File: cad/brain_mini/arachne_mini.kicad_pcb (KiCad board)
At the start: 4 copper layers, 92 x 60 mm, 86 parts, among them J1 12V IN, J13 5V PI, J2 L1 servo, J3 L2 servo, J4 L3 servo, J5 L4 servo, J6 L5 servo, J7 L6 servo, J8 USB-C PI, Q1 AOD4185, SW1 RESET, SW2 BOOT, U1 TPS54560B, U10 USBLC6-2SC6, U2 AMS1117-3.3, U3 ESP32-S3-WROOM-1-N16R8, U4 74AHCT1G126, U5 74LVC1G34, U6 74AHCT1G126, U7 74LVC1G34, U8 MPU-6050

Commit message: Mini board: 2x13 GPIO header with all 19 free ESP32-S3 GPIOs + I2C + power, IMU moved
Co-Authored-By: Claude Opus 5.5 <noreply@anthropic.com>
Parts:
- added J14: GPIO, arachne:PinHeader_2x13_P2.54mm_Vertical, F.Cu at (151.2, 93.5)
- moved C24 17.6 mm to (147.0, 87.0)
- moved C25 17.6 mm to (154.0, 87.0)
- moved C26 17.6 mm to (154.0, 83.0)
- moved C27 17.6 mm to (147.0, 83.0)
- moved R24 17.6 mm to (156.0, 83.0)
- moved R25 17.6 mm to (157.6, 83.0)
- moved U8 17.6 mm to (150.5, 85.0)
- moved D6 2.50 mm to (160.0, 117.5)
- moved D7 2.50 mm to (160.0, 121.5)
- moved R27 1.30 mm to (164.8, 118.5)
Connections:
- U3 pad 12: unconnected-(U3-IO8-Pad12) -> IO8
- U3 pad 15: unconnected-(U3-IO3-Pad15) -> IO3
- U3 pad 16: unconnected-(U3-IO46-Pad16) -> IO46
- U3 pad 20: unconnected-(U3-IO12-Pad20) -> IO12
- U3 pad 21: unconnected-(U3-IO13-Pad21) -> IO13
- U3 pad 22: unconnected-(U3-IO14-Pad22) -> IO14
- U3 pad 23: unconnected-(U3-IO21-Pad23) -> IO21
- U3 pad 24: unconnected-(U3-IO47-Pad24) -> IO47
- U3 pad 25: unconnected-(U3-IO48-Pad25) -> IO48
- U3 pad 26: unconnected-(U3-IO45-Pad26) -> IO45
- U3 pad 31: unconnected-(U3-IO38-Pad31) -> IO38
- U3 pad 32: unconnected-(U3-IO39-Pad32) -> IO39
- U3 pad 33: unconnected-(U3-IO40-Pad33) -> IO40
- U3 pad 34: unconnected-(U3-IO41-Pad34) -> IO41
- U3 pad 35: unconnected-(U3-IO42-Pad35) -> IO42
- U3 pad 36: unconnected-(U3-RXD0-Pad36) -> IO44
- U3 pad 37: unconnected-(U3-TXD0-Pad37) -> IO43
- U3 pad 7: unconnected-(U3-IO7-Pad7) -> IO7
- U3 pad 8: unconnected-(U3-IO15-Pad8) -> IO15
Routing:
- net IO44: track 0.00 -> 70.6 mm, vias 0 -> 1
- net IO40: track 0.00 -> 69.2 mm, vias 0 -> 1
- net IO42: track 0.00 -> 69.2 mm, vias 0 -> 1
- net IO43: track 0.00 -> 66.5 mm, vias 0 -> 1
- net IO41: track 0.00 -> 61.7 mm, vias 0 -> 1
- net IO39: track 0.00 -> 59.8 mm, vias 0 -> 1
- net IO38: track 0.00 -> 56.3 mm, vias 0 -> 2
- net IO48: track 0.00 -> 53.8 mm, vias 0 -> 1
- net IO45: track 0.00 -> 42.6 mm, vias 0 -> 2
- net IO21: track 0.00 -> 34.7 mm, vias 0 -> 2
- net IO14: track 0.00 -> 34.1 mm, vias 0 -> 3
- net IO47: track 0.00 -> 33.6 mm, vias 0 -> 2
- net IO46: track 0.00 -> 32.4 mm, vias 0 -> 1
- net IO13: track 0.00 -> 31.1 mm, vias 0 -> 2
- net IO7: track 0.00 -> 26.4 mm, vias 0 -> 1
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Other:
- board text added: "3V3"
- board text added: "5V"
- board text added: "GND"
- board text added: "GPIO"
- board text added: "IO12"
- board text added: "IO13"
- board text added: "IO14"
- board text added: "IO15"
- board text added: "IO21"
- board text added: "IO3"
- board text added: "IO38"
- board text added: "IO39"
- board text added: "IO40"
- board text added: "IO41"
- board text added: "IO42"
- board text added: "IO45"
- board text added: "IO46"
- board text added: "IO47"
- board text added: "IO48"
- board text added: "IO7"
- board text added: "IO8"
- board text added: "RX44"
- board text added: "SCL5"
- board text added: "SDA4"
- board text added: "TX43"
- board text removed: "ESP32-S3 v1.0"
- board text removed: "MINI"

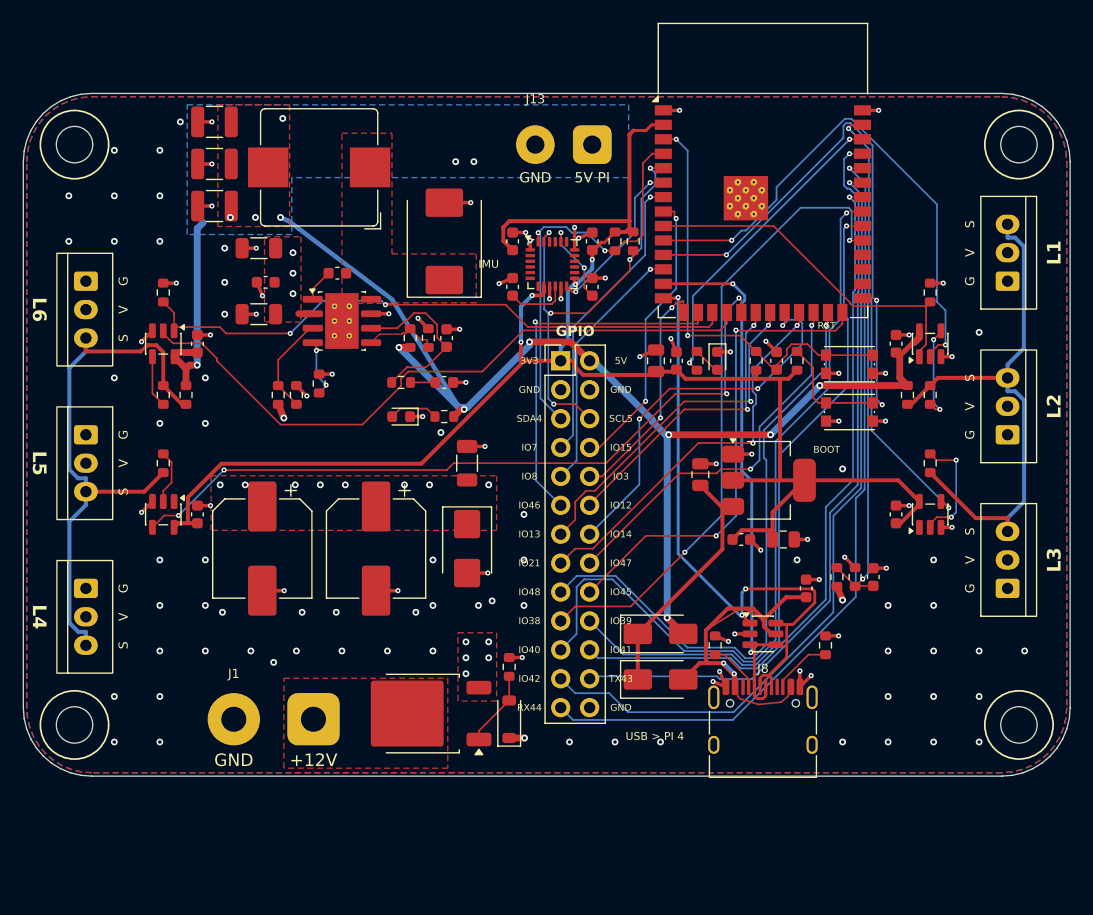
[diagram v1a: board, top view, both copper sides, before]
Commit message: Mini board: sensor strip (G-V-S per GPIO) on a 10 mm longer bottom edge, 2x Qwiic, USB-C moved to the new edge
Co-Authored-By: Claude Opus 5.5 <noreply@anthropic.com>
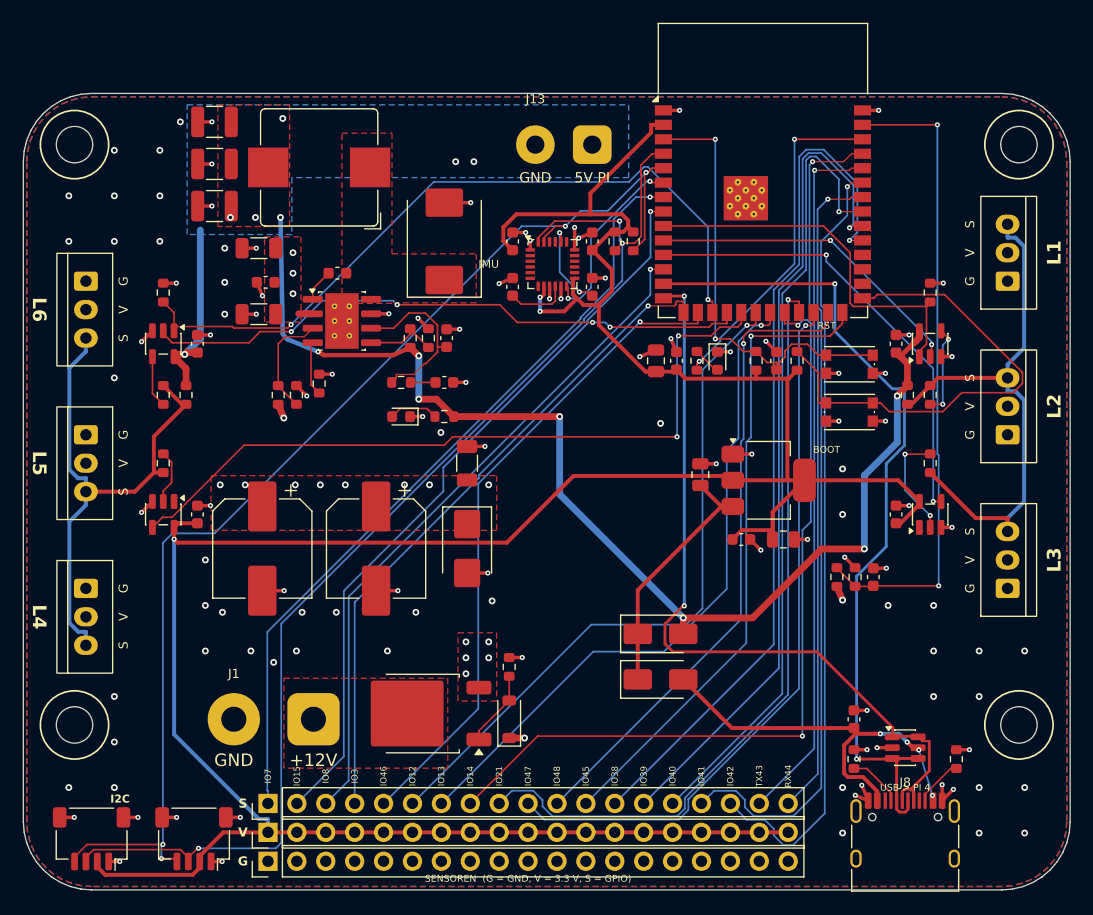
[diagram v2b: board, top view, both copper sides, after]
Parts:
- added J15: SENSOR V, arachne:PinHeader_1x19_P2.54mm_Vertical, F.Cu at (125.5, 134.9)
- added J16: SENSOR G, arachne:PinHeader_1x19_P2.54mm_Vertical, F.Cu at (125.5, 137.5)
- added J17: I2C, arachne:JST_SH_SM04B-SRSS-TB_1x04-1MP_P1.00mm_Horizontal, F.Cu at (110.0, 135.5)
- added J18: I2C, arachne:JST_SH_SM04B-SRSS-TB_1x04-1MP_P1.00mm_Horizontal, F.Cu at (119.0, 135.5)
- J14: value GPIO -> SENSOR S; footprint arachne:PinHeader_2x13_P2.54mm_Vertical -> arachne:PinHeader_1x19_P2.54mm_Vertical
- moved J14 46.6 mm to (125.5, 132.4), turned to 90 degrees
- moved U10 16.0 mm to (181.5, 127.5)
- moved J8 16.0 mm to (181.5, 136.2)
- moved R27 15.8 mm to (177.0, 128.5)
- moved R28 15.2 mm to (186.0, 128.5)
- moved C29 12.2 mm to (177.0, 125.0)
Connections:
- J14 pad 1: 3V3 -> IO7
- J14 pad 10: IO3 -> IO47
- J14 pad 11: IO46 -> IO48
- J14 pad 12: IO12 -> IO45
- J14 pad 13: IO13 -> IO38
- J14 pad 14: IO14 -> IO39
- J14 pad 15: IO21 -> IO40
- J14 pad 16: IO47 -> IO41
- J14 pad 17: IO48 -> IO42
- J14 pad 18: IO45 -> IO43
- J14 pad 19: IO38 -> IO44
- J14 pad 2: V5 -> IO15
- J14 pad 3: GND -> IO8
- J14 pad 4: GND -> IO3
- J14 pad 5: IMU_SDA -> IO46
- J14 pad 6: IMU_SCL -> IO12
- J14 pad 7: IO7 -> IO13
- J14 pad 8: IO15 -> IO14
- J14 pad 9: IO8 -> IO21
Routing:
- net 3V3: track 154.0 -> 256.6 mm, vias 4 -> 3
- net IMU_SDA: track 37.3 -> 105.8 mm, vias 2 -> 3
- net IMU_SCL: track 41.2 -> 105.5 mm, vias 5 -> 4
- net IO7: track 26.4 -> 69.1 mm
- net IO15: track 25.4 -> 66.0 mm, vias 2 -> 1
- net IO3: track 20.7 -> 58.8 mm, vias 2 -> 1
- net IO14: track 34.1 -> 71.9 mm, vias 3 -> 2
- net IO8: track 22.6 -> 59.9 mm
- net IO12: track 26.4 -> 60.9 mm, vias 2 -> 1
- net IO21: track 34.7 -> 68.8 mm, vias 2 -> 1
- net IO47: track 33.6 -> 63.6 mm, vias 2 -> 1
- net IO13: track 31.1 -> 59.5 mm, vias 2 -> 1
- net IO46: track 32.4 -> 57.8 mm
- net ESP_DM: track 48.5 -> 73.8 mm
- net ESP_IO0: track 21.7 -> 42.6 mm, vias 2 -> 0
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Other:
- board size 92 x 60 mm -> 92 x 70 mm
- board text added: "G"
- board text added: "I2C"
- board text added: "S"
- board text added: "SENSOREN (G = GND, V = 3.3 V, S = GPIO)"
- board text added: "V"
- board text removed: "3V3"
- board text removed: "5V"
- board text removed: "GND"
- board text removed: "GPIO"
- board text removed: "SCL5"
- board text removed: "SDA4"

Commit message: Mini board: servo headers are now Molex Mini-SPOX 5267-03A (chamfered, mates with the 5264 plug), real Molex in the BOM
Co-Authored-By: Claude Opus 5.5 <noreply@anthropic.com>
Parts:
- J2, J3, J4, J5, J6, J7: footprint arachne:Molex_5268-03A_1x03_P2.50mm_Vertical -> arachne:Molex_5267-03A_1x03_P2.50mm_Vertical
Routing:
- net 3V3: track 256.6 -> 231.7 mm, vias 3 -> 4
- net ESP_IO0: track 42.6 -> 21.6 mm, vias 0 -> 2
- net IO14: track 71.9 -> 57.4 mm, vias 2 -> 1
- net IO39: track 73.4 -> 62.4 mm
- net IMU_SDA: track 105.8 -> 116.7 mm, vias 3 -> 5
- net VSENSE: track 56.8 -> 46.3 mm
- net BUS_A: track 49.6 -> 41.0 mm
- net IO40: track 70.2 -> 61.6 mm
- net IO47: track 63.6 -> 55.7 mm
- net IO42: track 69.0 -> 61.3 mm
- net IO41: track 68.7 -> 61.3 mm
- net LED_ESP: track 29.9 -> 37.0 mm
- net IO48: track 56.7 -> 63.8 mm, vias 1 -> 2
- net IO21: track 68.8 -> 61.8 mm
- net IO44: track 61.2 -> 68.1 mm
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
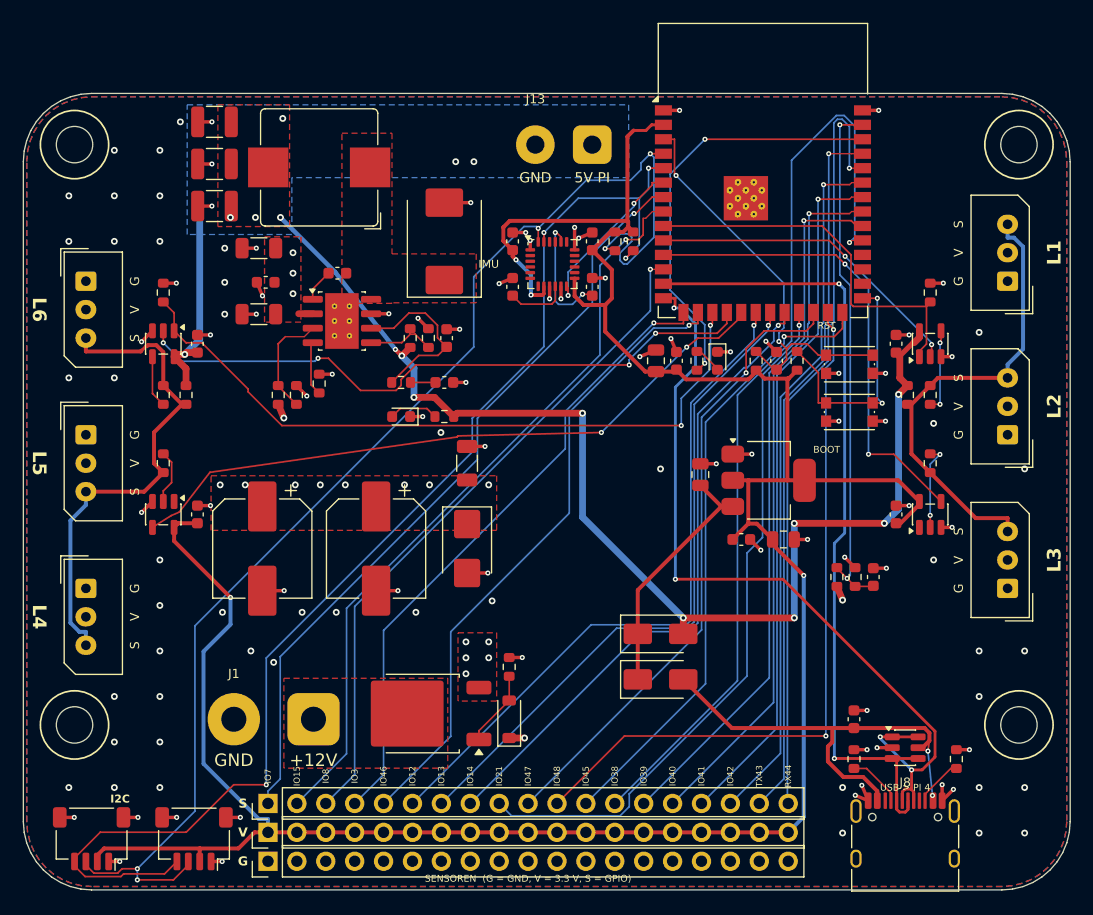
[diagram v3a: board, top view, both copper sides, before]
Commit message: Mini board: MPU-6050 moved to the exact robot centre (0,0)
Co-Authored-By: Claude Opus 5.5 <noreply@anthropic.com>
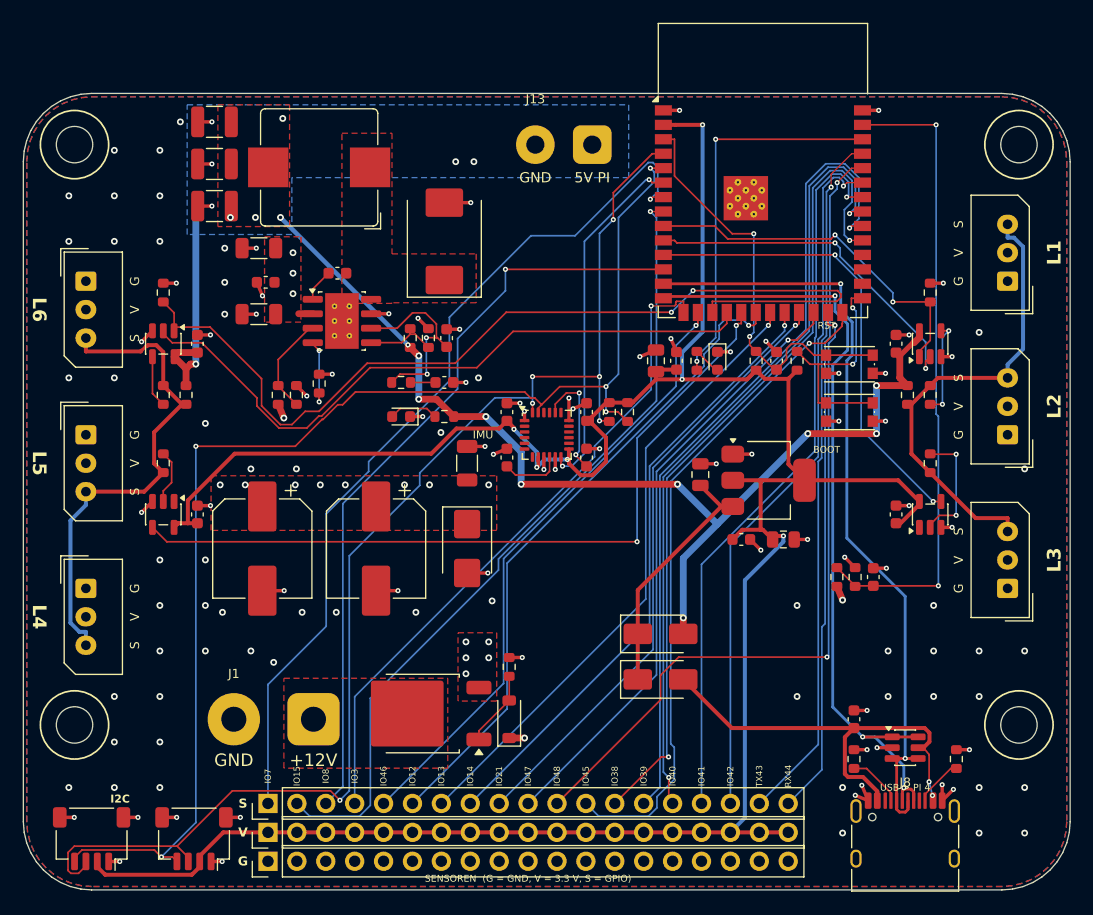
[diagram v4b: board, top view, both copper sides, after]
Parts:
- moved C24 15.0 mm to (146.5, 102.0)
- moved C25 15.0 mm to (153.5, 102.0)
- moved C26 15.0 mm to (153.5, 98.0)
- moved C27 15.0 mm to (146.5, 98.0)
- moved R24 15.0 mm to (155.5, 98.0)
- moved R25 15.0 mm to (157.1, 98.0)
- moved U8 15.0 mm to (150.0, 100.0)
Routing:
- net DE_B: track 62.2 -> 84.2 mm
- net IMU_INT: track 14.8 -> 31.2 mm
- net VSENSE: track 46.3 -> 56.7 mm
- net IO39: track 62.4 -> 72.2 mm
- net IO7: track 68.4 -> 77.7 mm
- net IO38: track 82.2 -> 73.1 mm, vias 1 -> 2
- net IO44: track 68.1 -> 59.1 mm
- net V5: track 123.1 -> 114.3 mm, vias 14 -> 15
- net RX_B: track 58.5 -> 67.2 mm
- net IO40: track 61.6 -> 69.5 mm, vias 1 -> 2
- net IO21: track 61.8 -> 54.2 mm
- net IO8: track 59.9 -> 67.4 mm
- net IO15: track 66.7 -> 71.3 mm
- net IMU_SDA: track 116.7 -> 112.8 mm, vias 5 -> 6
- net IMU_SCL: track 110.2 -> 114.0 mm, vias 4 -> 5
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
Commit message: Name Kobe Vanrobaeys on silkscreen/schematic, fresh JLC fab files for brain_mini
Co-Authored-By: Claude Opus 5.5 <noreply@anthropic.com>
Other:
- board text added: "Kobe Vanrobaeys · maakleerplek · 2026"
- board text removed: "Kobe Van Robaeys · maakleerplek · 2026"
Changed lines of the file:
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@@
 		)
 	)
-	(gr_text "Kobe Van Robaeys  ·  maakleerplek  ·  2026"
+	(gr_text "Kobe Vanrobaeys  ·  maakleerplek  ·  2026"
 		(at 167 110.5 0)
 		(layer "B.SilkS")

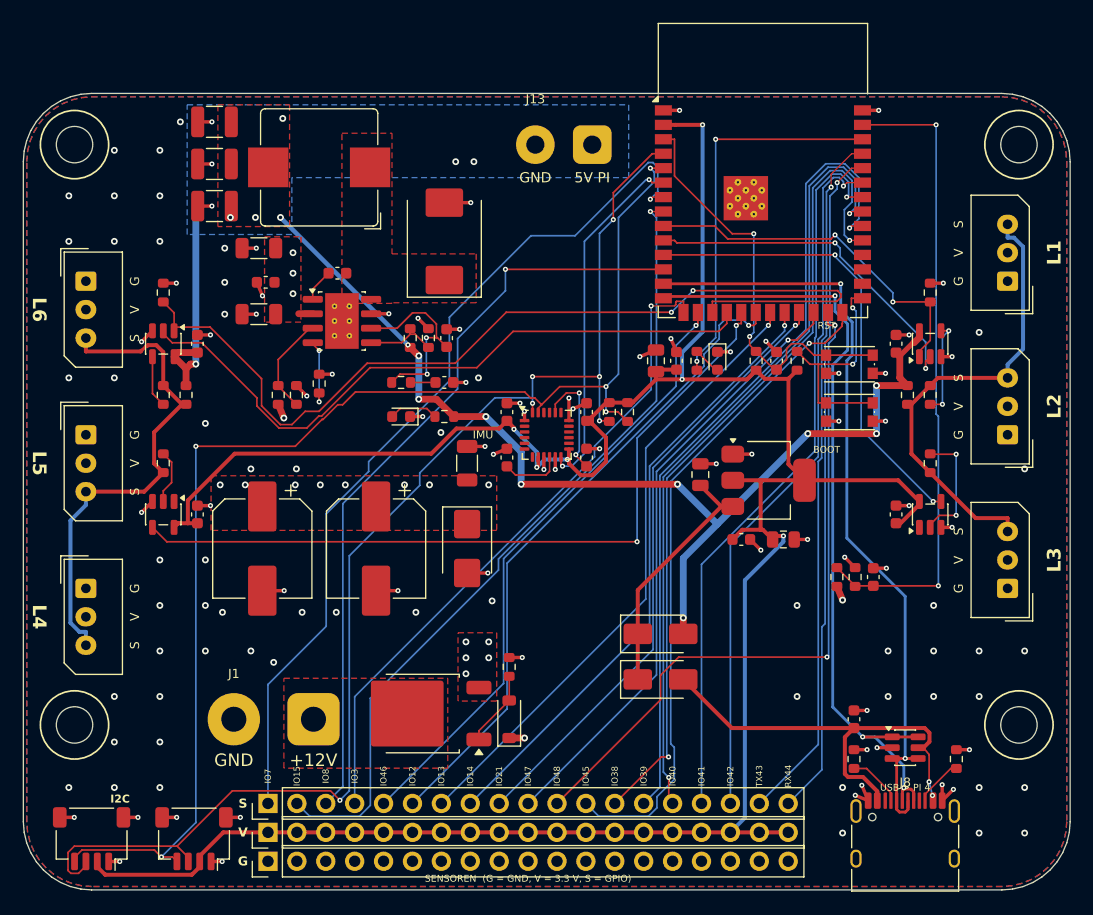
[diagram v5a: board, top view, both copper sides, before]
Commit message: brain_mini v4 price pass: JLC basic parts (buck network, caps, SS54, LEDs), LSM6DS3TR-C IMU, hand-solder parts DNP, JLC rotation corrections in the CPL
Co-Authored-By: Claude Opus 5.5 <noreply@anthropic.com>
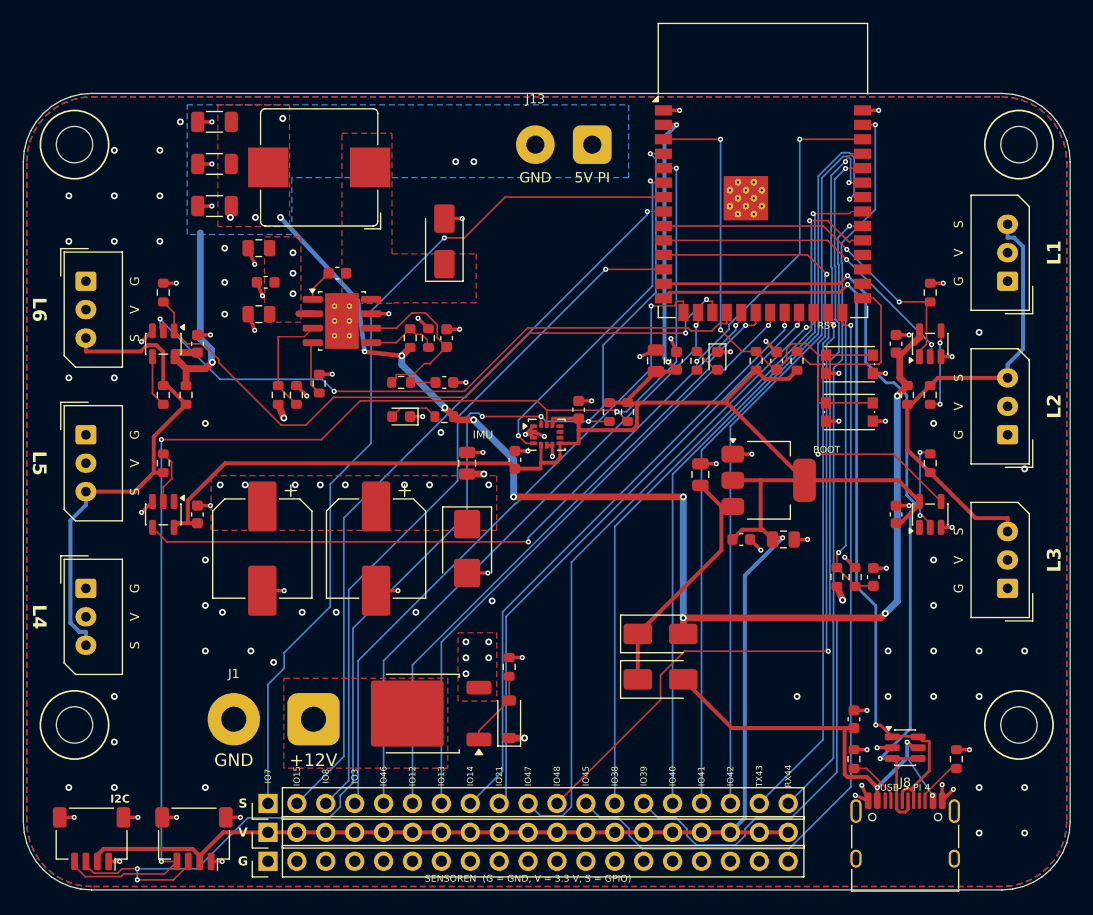
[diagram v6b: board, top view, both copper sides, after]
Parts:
- removed C25: 2n2, arachne:C_0603_1608Metric
- removed C27: 10n, arachne:C_0603_1608Metric
- C10, C11, C9: footprint arachne:C_1210_3225Metric -> arachne:C_1206_3216Metric
- C3, C5, C6: footprint arachne:C_1206_3216Metric -> arachne:C_0805_2012Metric
- D4: value B560C -> SS54; footprint arachne:D_SMC -> arachne:D_SMA
- D5: value groen 5V -> LED 5V
- D8: value blauw ESP -> LED ESP
- R4: value 442k -> 470k
- R5: value 90.9k -> 100k
- R6: value 243k -> 220k
- R7: value 53.6k -> 27k
- R8: value 10.2k -> 5k1
- R9: value 16.9k -> 15k
- U8: value MPU-6050 -> LSM6DS3TR-C; footprint arachne:InvenSense_QFN-24_4x4mm_P0.5mm -> arachne:LGA-14_3x2.5mm_P0.5mm_LayoutBorder3x4y
- moved C24 0.73 mm to (147.2, 102.2)
- moved C26 0.73 mm to (152.8, 97.8)
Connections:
- C24 pad 1: IMU_REG -> 3V3
- U8 pad 10: IMU_REG -> unconnected-(U8-NC-Pad10)
- U8 pad 11: GND -> unconnected-(U8-NC-Pad11)
- U8 pad 12: IMU_INT -> 3V3
- U8 pad 13: 3V3 -> IMU_SCL
- U8 pad 14: unconnected-(U8-NC-Pad14) -> IMU_SDA
- U8 pad 2: unconnected-(U8-NC-Pad2) -> GND
- U8 pad 3: unconnected-(U8-NC-Pad3) -> GND
- U8 pad 4: unconnected-(U8-NC-Pad4) -> IMU_INT
- U8 pad 5: unconnected-(U8-NC-Pad5) -> 3V3
- U8 pad 6: unconnected-(U8-AUX_DA-Pad6) -> GND
- U8 pad 7: unconnected-(U8-AUX_CL-Pad7) -> GND
- U8 pad 9: GND -> unconnected-(U8-INT2-Pad9)
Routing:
- net DE_B: track 84.2 -> 60.1 mm
- net V5: track 114.3 -> 127.7 mm, vias 15 -> 14
- net IO45: track 58.4 -> 69.9 mm
- net VSENSE: track 56.7 -> 45.7 mm
- net IMU_CP: track 10.2 -> 0.00 mm, vias 2 -> 0
- net IO38: track 73.1 -> 64.0 mm, vias 2 -> 1
- net IO40: track 69.5 -> 61.5 mm, vias 2 -> 1
- net RX_B: track 67.2 -> 61.5 mm
- net IMU_REG: track 5.46 -> 0.00 mm
- net IO8: track 67.4 -> 62.2 mm
- net IO15: track 71.3 -> 66.2 mm
- net LED_ESP: track 33.9 -> 29.6 mm
- net IMU_SCL: track 114.0 -> 118.3 mm, vias 5 -> 4
- net ESP_DM: track 68.7 -> 72.8 mm
- net IO41: track 64.6 -> 68.6 mm
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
